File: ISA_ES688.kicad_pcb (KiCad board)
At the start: 4 copper layers, 104.1 x 99.1 mm, 115 parts, among them J1 ISA BUS, J2 Interrupt Select, J3 Address Select, J4 DMA Select, J5 Joystick/MIDI, J6 LINE OUT, J7 MIC, J8 LINE IN, J9 SPKR OUT, U1 74LS14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

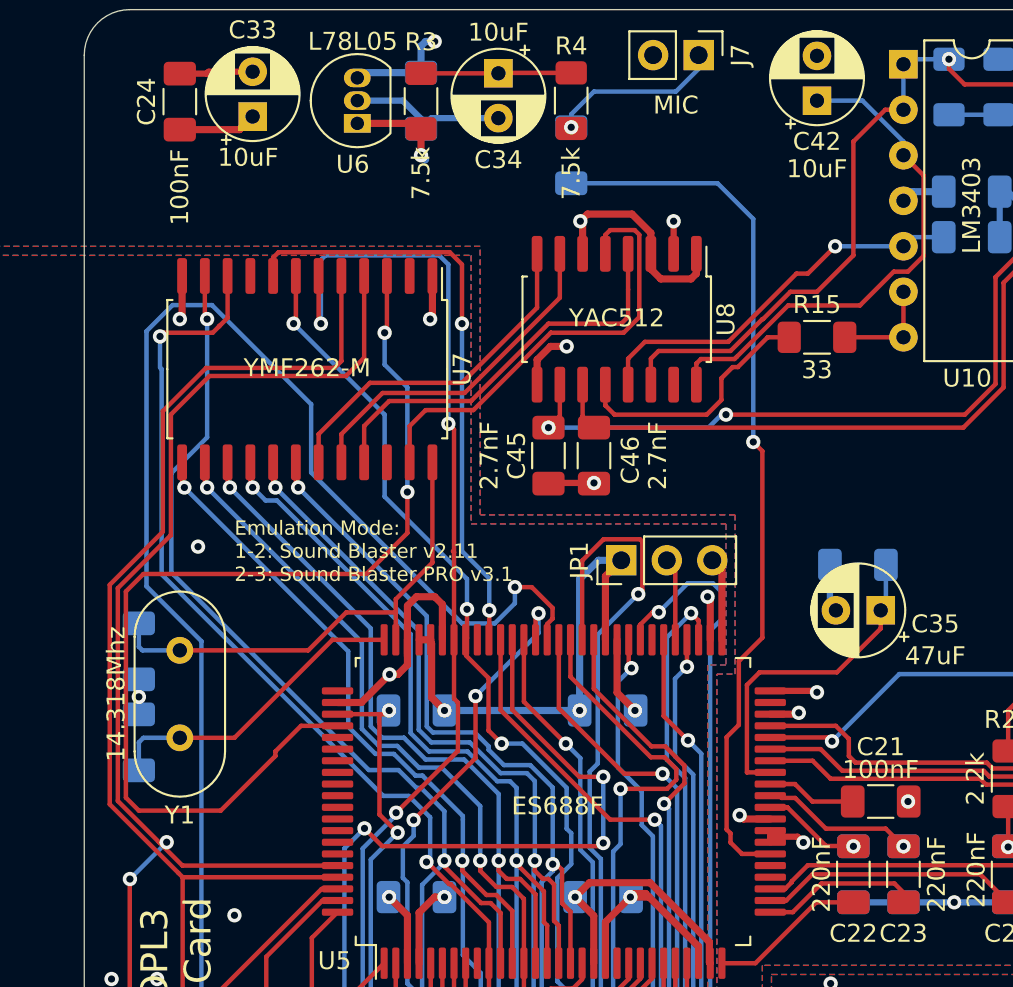
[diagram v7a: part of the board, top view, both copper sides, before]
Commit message: Enlarged footprints for YAC and OPL, again
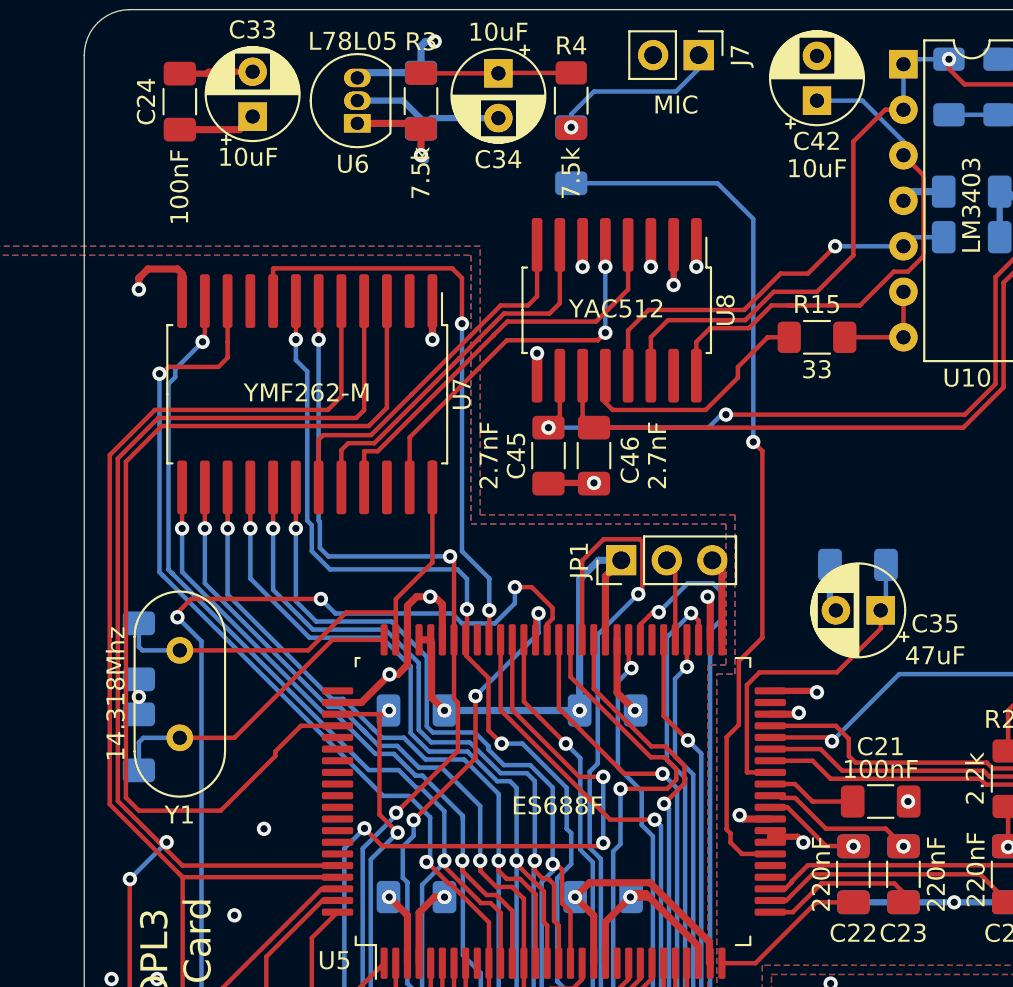
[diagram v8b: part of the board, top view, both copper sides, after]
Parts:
- moved U7 1.40 mm to (223.3, 125.6)
- moved U8 0.50 mm to (240.5, 120.9)
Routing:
- net Net-(JP3-Pad2): track 112.0 -> 84.6 mm, vias 1 -> 3
- net VDDA: track 102.0 -> 91.0 mm, vias 5 -> 7
- net /~IOW: track 122.2 -> 113.3 mm
- net Net-(U7-Pad23): track 25.1 -> 19.8 mm, vias 0 -> 2
- net /~FMRSTB: track 57.9 -> 54.9 mm, vias 2 -> 0
- net /~IOR: track 105.0 -> 107.7 mm
- net GNDA: track 399.0 -> 401.2 mm
- net Net-(U7-Pad20): track 19.4 -> 20.9 mm
- net VCC: track 320.2 -> 318.8 mm, vias 7 -> 8
- net Net-(U7-Pad19): track 19.7 -> 21.0 mm
- net /ES-D1: track 113.7 -> 112.5 mm
- net /ES-D0: track 112.1 -> 110.9 mm
- net /ES-D7: track 108.9 -> 109.9 mm
- net /ES-D6: track 109.5 -> 110.5 mm
- net /ES-D4: track 119.7 -> 119.0 mm
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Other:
- board text removed: "Emulation Mode: 1-2: Sound Blaster v2.11 2-3: Sound Blaster PRO v3.1"
